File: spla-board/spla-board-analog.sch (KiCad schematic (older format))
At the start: 91 parts, among them J13 J_ANALOG, J14 J_AREF, J8 J_AREF_AMP, U51 ADC1173, U52 ADC1173, U53 ADC1173, U61 LMH6611, U62 LMH6611, U63 LMH6611, U74 LMH6611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

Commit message: schematic: Add Digikey and ManufacturerId fields to big components.
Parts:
- U51, U52, U53: Digikey (none) -> 296-35234-1-ND; Manufacturer Id (none) -> ADC1173CIMTCX/NOPB
- U61, U62, U63, U74, U75: Digikey (none) -> 296-41441-1-ND; Manufacturer Id (none) -> LMH6611MK/NOPB
- U76: Digikey (none) -> 296-40673-1-ND; Manufacturer Id (none) -> TLV73333PDBVR
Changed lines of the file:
@@
 F 2 "Package_SO:TSSOP-24_4.4x7.8mm_P0.65mm" H 14300 2550 50  0001 C CNN
 F 3 "http://www.ti.com/lit/ds/symlink/adc1173.pdf" H 14300 2550 50  0001 C CNN
+F 4 "296-35234-1-ND" H 14300 2550 50  0001 C CNN "Digikey"
+F 5 "ADC1173CIMTCX/NOPB" H 14300 2550 50  0001 C CNN "Manufacturer Id"
 	1    14300 2550
 	1    0    0    -1
@@
 F 2 "Package_SO:TSSOP-24_4.4x7.8mm_P0.65mm" H 14300 8650 50  0001 C CNN
 F 3 "http://www.ti.com/lit/ds/symlink/adc1173.pdf" H 14300 8650 50  0001 C CNN
+F 4 "296-35234-1-ND" H 14300 8650 50  0001 C CNN "Digikey"
+F 5 "ADC1173CIMTCX/NOPB" H 14300 8650 50  0001 C CNN "Manufacturer Id"
 	1    14300 8650
 	1    0    0    -1
@@
 F 2 "Package_SO:TSSOP-24_4.4x7.8mm_P0.65mm" H 14300 5600 50  0001 C CNN
 F 3 "http://www.ti.com/lit/ds/symlink/adc1173.pdf" H 14300 5600 50  0001 C CNN
+F 4 "296-35234-1-ND" H 14300 5600 50  0001 C CNN "Digikey"
+F 5 "ADC1173CIMTCX/NOPB" H 14300 5600 50  0001 C CNN "Manufacturer Id"
 	1    14300 5600
 	1    0    0    -1
@@
 F 2 "Package_TO_SOT_SMD:TSOT-23-6" H 9650 8000 50  0001 L CNN
 F 3 "http://www.ti.com/lit/ds/symlink/lmh6612.pdf" H 9700 8400 50  0001 C CNN
+F 4 "296-41441-1-ND" H 9550 8250 50  0001 C CNN "Digikey"
+F 5 "LMH6611MK/NOPB" H 9550 8250 50  0001 C CNN "Manufacturer Id"
 	1    9550 8250
 	1    0    0    -1
@@
 F 2 "Package_TO_SOT_SMD:TSOT-23-6" H 9650 1900 50  0001 L CNN
 F 3 "http://www.ti.com/lit/ds/symlink/lmh6612.pdf" H 9700 2300 50  0001 C CNN
+F 4 "296-41441-1-ND" H 9550 2150 50  0001 C CNN "Digikey"
+F 5 "LMH6611MK/NOPB" H 9550 2150 50  0001 C CNN "Manufacturer Id"
 	1    9550 2150
 	1    0    0    -1
@@
 F 2 "Package_TO_SOT_SMD:TSOT-23-6" H 9650 4950 50  0001 L CNN
 F 3 "http://www.ti.com/lit/ds/symlink/lmh6612.pdf" H 9700 5350 50  0001 C CNN
+F 4 "296-41441-1-ND" H 9550 5200 50  0001 C CNN "Digikey"
+F 5 "LMH6611MK/NOPB" H 9550 5200 50  0001 C CNN "Manufacturer Id"
 	1    9550 5200
 	1    0    0    -1
@@
 F 2 "Package_TO_SOT_SMD:TSOT-23-6" H 4400 7100 50  0001 L CNN
 F 3 "http://www.ti.com/lit/ds/symlink/lmh6612.pdf" H 4450 7500 50  0001 C CNN
+F 4 "296-41441-1-ND" H 4300 7350 50  0001 C CNN "Digikey"
+F 5 "LMH6611MK/NOPB" H 4300 7350 50  0001 C CNN "Manufacturer Id"
 	1    4300 7350
 	1    0    0    -1
@@
 F 2 "Package_TO_SOT_SMD:TSOT-23-6" H 4400 9650 50  0001 L CNN
 F 3 "http://www.ti.com/lit/ds/symlink/lmh6612.pdf" H 4450 10050 50  0001 C CNN
+F 4 "296-41441-1-ND" H 4300 9900 50  0001 C CNN "Digikey"
+F 5 "LMH6611MK/NOPB" H 4300 9900 50  0001 C CNN "Manufacturer Id"
 	1    4300 9900
 	1    0    0    -1
@@
 F 2 "Package_TO_SOT_SMD:SOT-23-5" H 2000 7100 50  0001 C CNN
 F 3 "http://www.ti.com/lit/ds/symlink/tlv733p.pdf" H 2100 6650 50  0001 C CNN
+F 4 "296-40673-1-ND" H 2000 6900 50  0001 C CNN "Digikey"
+F 5 "TLV73333PDBVR" H 2000 6900 50  0001 C CNN "Manufacturer Id"
 	1    2000 6900
 	1    0    0    -1

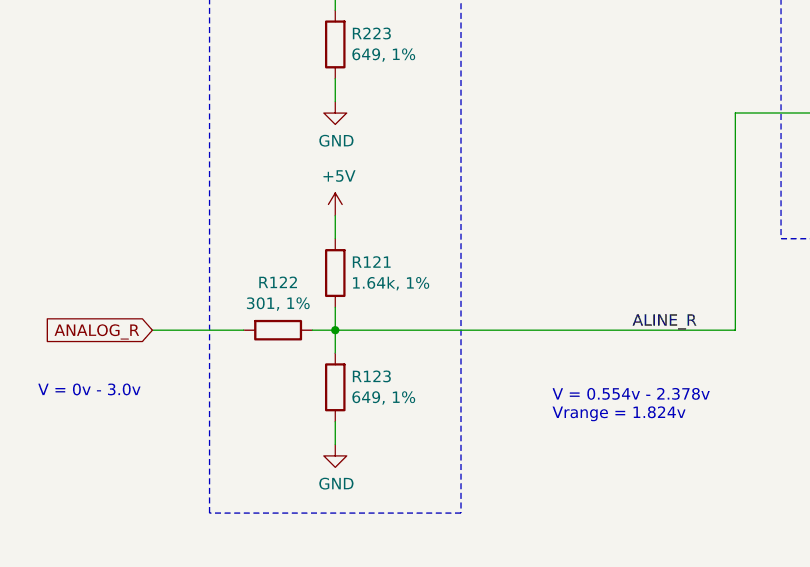
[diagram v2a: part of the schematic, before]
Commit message: schematic: Fix typo'd resistor value.
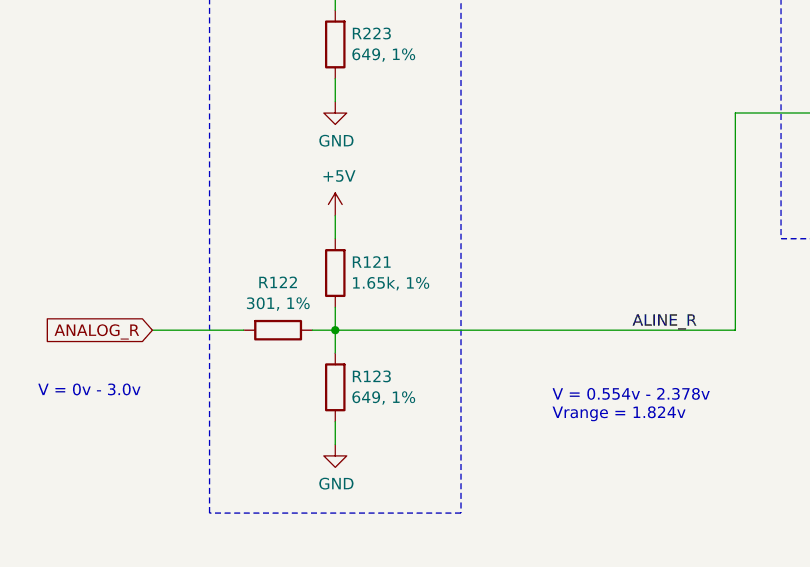
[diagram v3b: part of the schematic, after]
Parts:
- R121: value 1.64k, 1% -> 1.65k, 1%
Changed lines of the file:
@@
 P 2050 4250
 F 0 "R121" H 1980 4204 50  0000 R CNN
-F 1 "1.64k, 1%" H 1980 4295 50  0000 R CNN
+F 1 "1.65k, 1%" H 1980 4295 50  0000 R CNN
 F 2 "Resistor_SMD:R_0603_1608Metric" V 1980 4250 50  0001 C CNN
 F 3 "~" H 2050 4250 50  0001 C CNN

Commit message: schematic: Set 'N/A' for test points and holes 'parts'.
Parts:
- TP3, TP4: Digikey (none) -> N/A; Manufacturer Id (none) -> N/A
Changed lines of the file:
@@
 F 2 "TestPoint:TestPoint_Pad_D1.0mm" H 6400 8700 50  0001 C CNN
 F 3 "~" H 6400 8700 50  0001 C CNN
+F 4 "N/A" H 6200 8700 50  0001 C CNN "Digikey"
+F 5 "N/A" H 6200 8700 50  0001 C CNN "Manufacturer Id"
 	1    6200 8700
 	1    0    0    -1
@@
 F 2 "TestPoint:TestPoint_Pad_D1.0mm" H 6400 8900 50  0001 C CNN
 F 3 "~" H 6400 8900 50  0001 C CNN
+F 4 "N/A" H 6200 8900 50  0001 C CNN "Digikey"
+F 5 "N/A" H 6200 8900 50  0001 C CNN "Manufacturer Id"
 	1    6200 8900
 	-1   0    0    1

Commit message: schematic: Add part numbers for pinheaders (albeit that these are breakaways, and it's not one-per-part).
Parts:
- J13, J14, J8: Digikey (none) -> S2011EC-40-ND; Manufacturer Id (none) -> PRPC040DAAN-RC
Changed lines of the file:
@@
 F 2 "Connector_PinHeader_2.54mm:PinHeader_2x04_P2.54mm_Vertical" H 2100 8850 50  0001 C CNN
 F 3 "~" H 2100 8850 50  0001 C CNN
+F 4 "S2011EC-40-ND" H 2100 8850 50  0001 C CNN "Digikey"
+F 5 "PRPC040DAAN-RC" H 2100 8850 50  0001 C CNN "Manufacturer Id"
 	1    2100 8850
 	1    0    0    -1
@@
 F 2 "Connector_PinHeader_2.54mm:PinHeader_2x03_P2.54mm_Vertical" H 6250 3000 50  0001 C CNN
 F 3 "~" H 6250 3000 50  0001 C CNN
+F 4 "S2011EC-40-ND" H 6250 3000 50  0001 C CNN "Digikey"
+F 5 "PRPC040DAAN-RC" H 6250 3000 50  0001 C CNN "Manufacturer Id"
 	1    6250 3000
 	1    0    0    -1
@@
 F 2 "Connector_PinHeader_2.54mm:PinHeader_2x02_P2.54mm_Vertical" H 5800 8800 50  0001 C CNN
 F 3 "~" H 5800 8800 50  0001 C CNN
+F 4 "S2011EC-40-ND" H 5800 8800 50  0001 C CNN "Digikey"
+F 5 "PRPC040DAAN-RC" H 5800 8800 50  0001 C CNN "Manufacturer Id"
 	1    5800 8800
 	1    0    0    -1

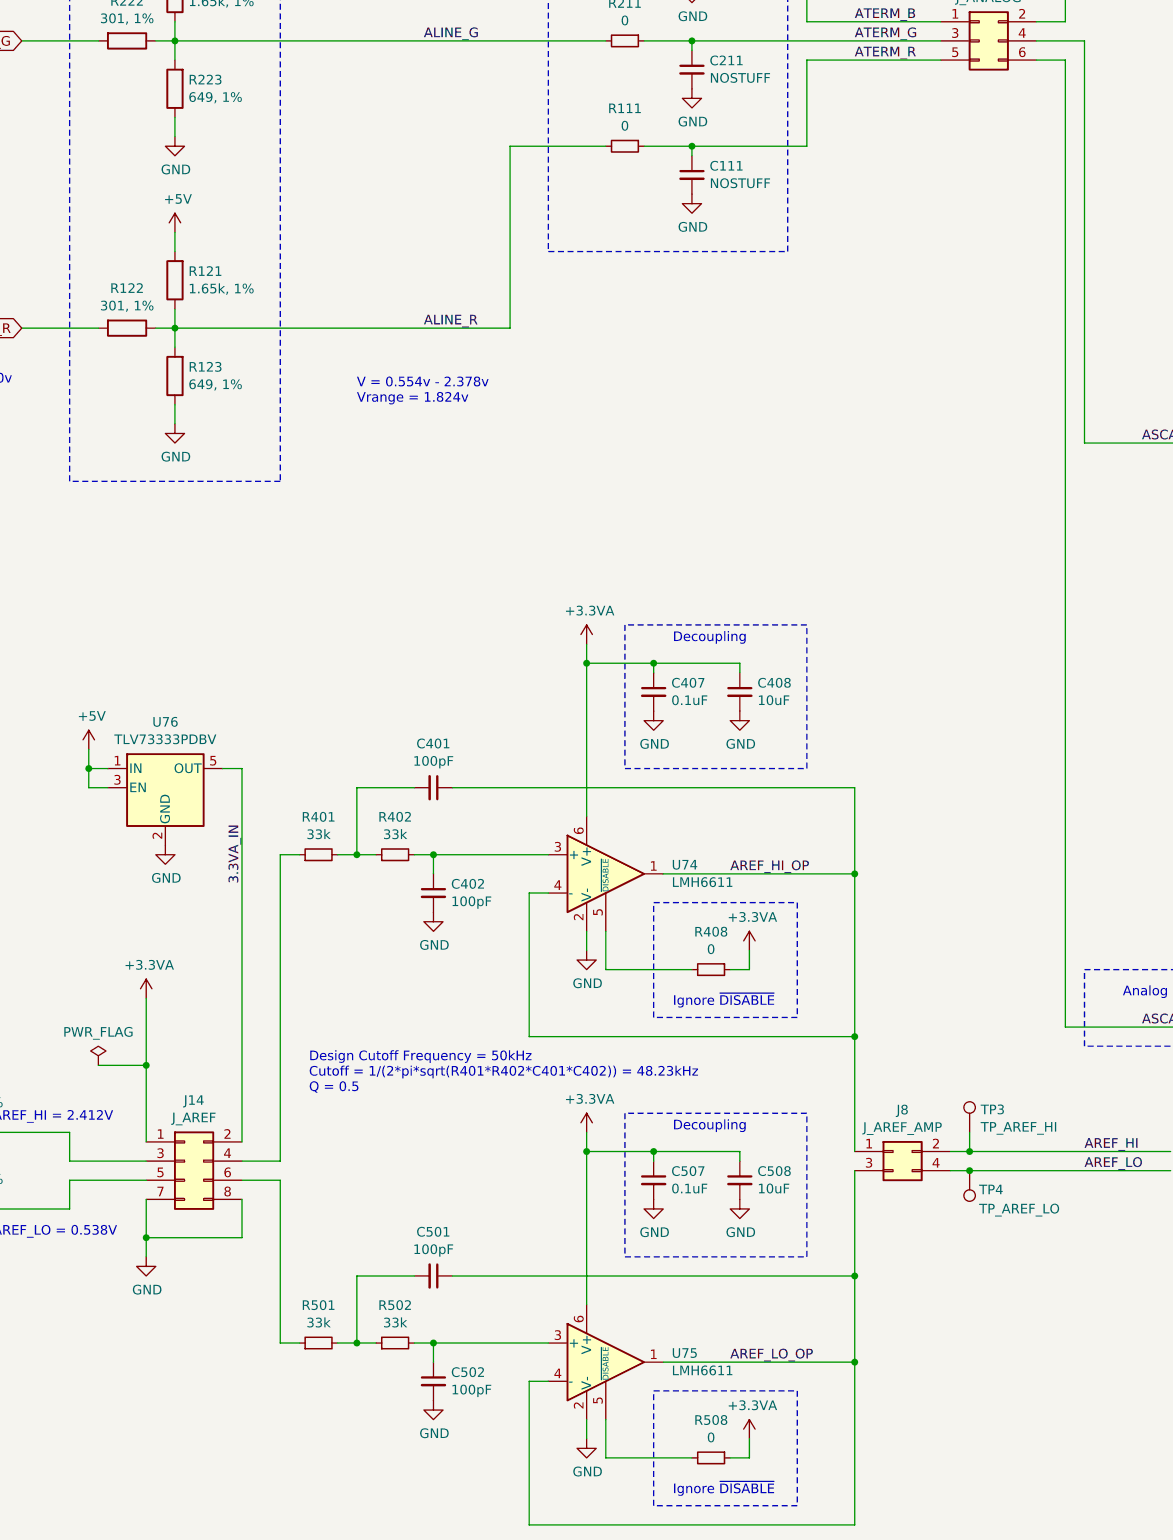
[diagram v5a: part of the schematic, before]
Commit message: schematic/pcb: Add BoM-only symbols.
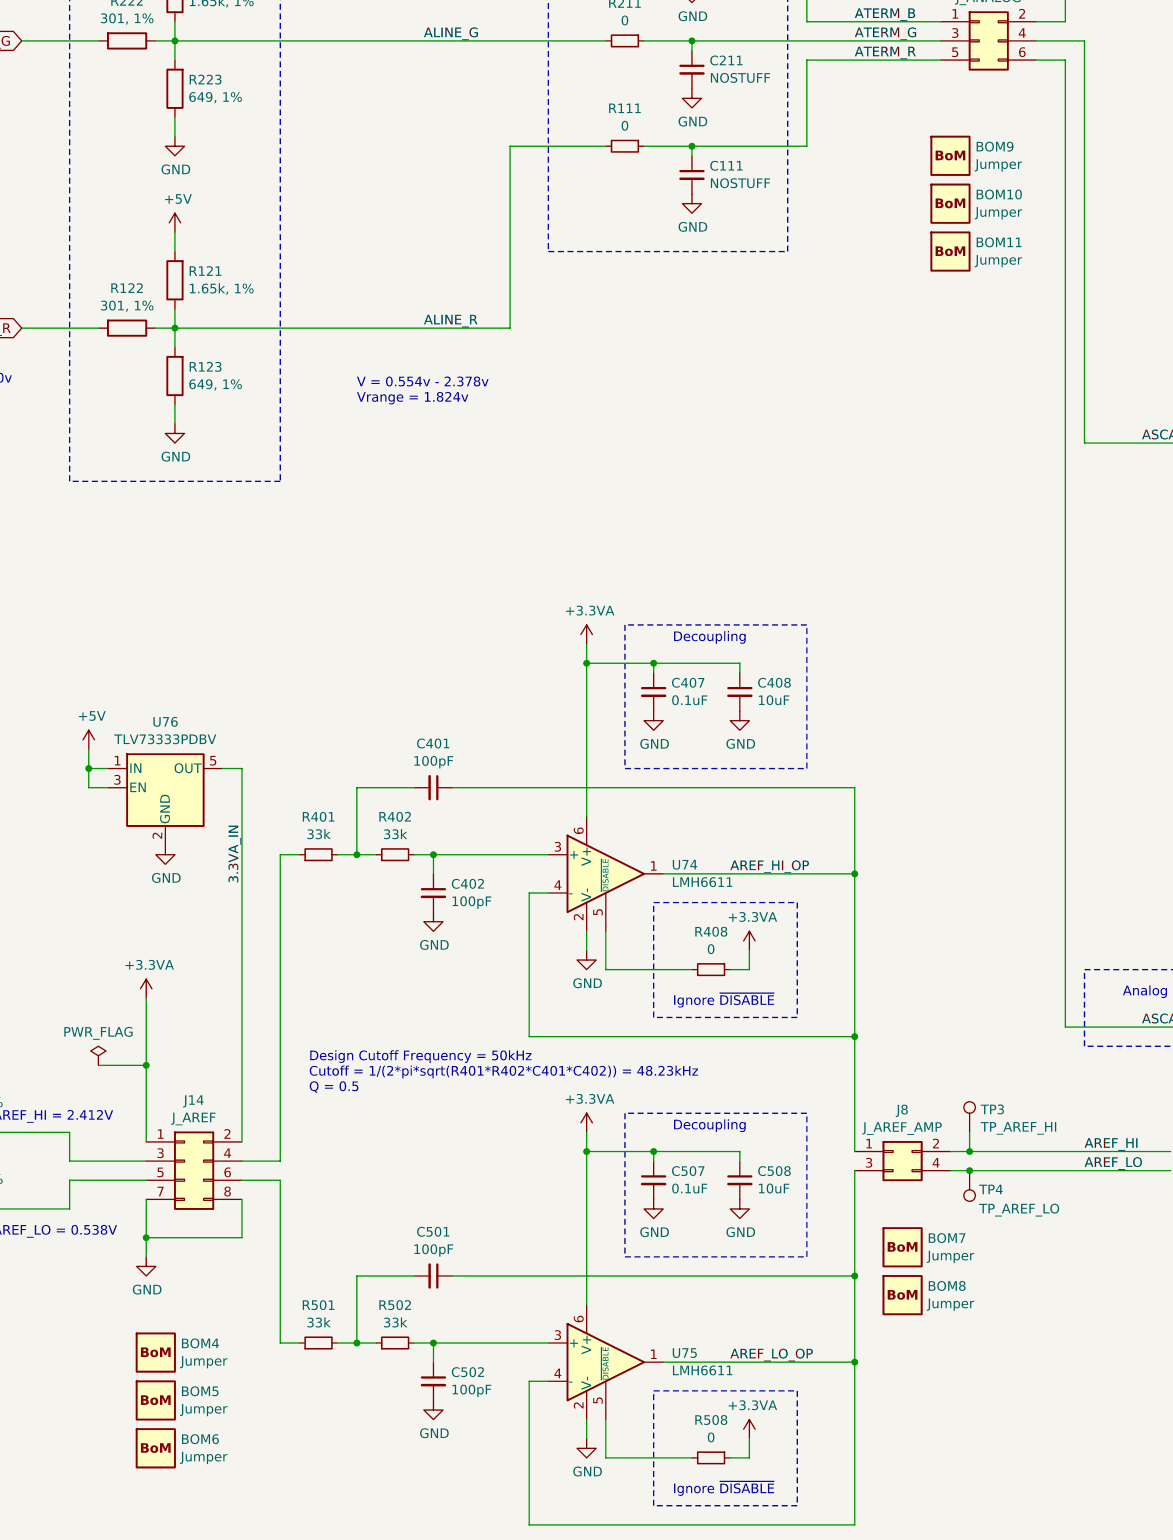
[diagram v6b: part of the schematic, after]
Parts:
- added BOM10, BOM11, BOM4, BOM5, BOM6, BOM7, BOM8, BOM9: Jumper, SPLA:BoM, symbol SPLA:BomExtra
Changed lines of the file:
@@
 	4550 8800 5000 8800
 Connection ~ 4550 8800
+$Comp
+L SPLA:BomExtra BOM?
+U 1 1 5EB18261
+P 1950 9850
+AR Path="/5E50E589/5EB18261" Ref="BOM?"  Part="1"
+AR Path="/5E520B87/5EB18261" Ref="BOM4"  Part="1"
+F 0 "BOM4" H 2080 9896 50  0000 L CNN
+F 1 "Jumper" H 2080 9805 50  0000 L CNN
+F 2 "SPLA:BoM" H 1950 9850 50  0001 C CNN
+F 3 "" H 1950 9850 50  0001 C CNN
+F 4 "S9337-ND" H 1950 9850 50  0001 C CNN "Digikey"
+F 5 "QPC02SXGN-RC" H 1950 9850 50  0001 C CNN "Manufacturer Id"
+	1    1950 9850
+	1    0    0    -1
+$EndComp
+$Comp
+L SPLA:BomExtra BOM?
+U 1 1 5EB36CC8
+P 1950 10100
+AR Path="/5E50E589/5EB36CC8" Ref="BOM?"  Part="1"
+AR Path="/5E520B87/5EB36CC8" Ref="BOM5"  Part="1"
+F 0 "BOM5" H 2080 10146 50  0000 L CNN
+F 1 "Jumper" H 2080 10055 50  0000 L CNN
+F 2 "SPLA:BoM" H 1950 10100 50  0001 C CNN
+F 3 "" H 1950 10100 50  0001 C CNN
+F 4 "S9337-ND" H 1950 10100 50  0001 C CNN "Digikey"
+F 5 "QPC02SXGN-RC" H 1950 10100 50  0001 C CNN "Manufacturer Id"
+	1    1950 10100
+	1    0    0    -1
+$EndComp
+$Comp
+L SPLA:BomExtra BOM?
+U 1 1 5EB558F5
+P 1950 10350
+AR Path="/5E50E589/5EB558F5" Ref="BOM?"  Part="1"
+AR Path="/5E520B87/5EB558F5" Ref="BOM6"  Part="1"
+F 0 "BOM6" H 2080 10396 50  0000 L CNN
+F 1 "Jumper" H 2080 10305 50  0000 L CNN
+F 2 "SPLA:BoM" H 1950 10350 50  0001 C CNN
+F 3 "" H 1950 10350 50  0001 C CNN
+F 4 "S9337-ND" H 1950 10350 50  0001 C CNN "Digikey"
+F 5 "QPC02SXGN-RC" H 1950 10350 50  0001 C CNN "Manufacturer Id"
+	1    1950 10350
+	1    0    0    -1
+$EndComp
+$Comp
+L SPLA:BomExtra BOM?
+U 1 1 5EB744FF
+P 5850 9300
+AR Path="/5E50E589/5EB744FF" Ref="BOM?"  Part="1"
+AR Path="/5E520B87/5EB744FF" Ref="BOM7"  Part="1"
+F 0 "BOM7" H 5980 9346 50  0000 L CNN
+F 1 "Jumper" H 5980 9255 50  0000 L CNN
+F 2 "SPLA:BoM" H 5850 9300 50  0001 C CNN
+F 3 "" H 5850 9300 50  0001 C CNN
+F 4 "S9337-ND" H 5850 9300 50  0001 C CNN "Digikey"
+F 5 "QPC02SXGN-RC" H 5850 9300 50  0001 C CNN "Manufacturer Id"
+	1    5850 9300
+	1    0    0    -1
+$EndComp
+$Comp
+L SPLA:BomExtra BOM?
+U 1 1 5EB7450B
+P 5850 9550
+AR Path="/5E50E589/5EB7450B" Ref="BOM?"  Part="1"
+AR Path="/5E520B87/5EB7450B" Ref="BOM8"  Part="1"
+F 0 "BOM8" H 5980 9596 50  0000 L CNN
+F 1 "Jumper" H 5980 9505 50  0000 L CNN
+F 2 "SPLA:BoM" H 5850 9550 50  0001 C CNN
+F 3 "" H 5850 9550 50  0001 C CNN
+F 4 "S9337-ND" H 5850 9550 50  0001 C CNN "Digikey"
+F 5 "QPC02SXGN-RC" H 5850 9550 50  0001 C CNN "Manufacturer Id"
+	1    5850 9550
+	1    0    0    -1
+$EndComp
+$Comp
+L SPLA:BomExtra BOM?
+U 1 1 5EB936B5
+P 6100 3600
+AR Path="/5E50E589/5EB936B5" Ref="BOM?"  Part="1"
+AR Path="/5E520B87/5EB936B5" Ref="BOM9"  Part="1"
+F 0 "BOM9" H 6230 3646 50  0000 L CNN
+F 1 "Jumper" H 6230 3555 50  0000 L CNN
+F 2 "SPLA:BoM" H 6100 3600 50  0001 C CNN
+F 3 "" H 6100 3600 50  0001 C CNN
+F 4 "S9337-ND" H 6100 3600 50  0001 C CNN "Digikey"
+F 5 "QPC02SXGN-RC" H 6100 3600 50  0001 C CNN "Manufacturer Id"
+	1    6100 3600
+	1    0    0    -1
+$EndComp
+$Comp
+L SPLA:BomExtra BOM?
+U 1 1 5EBB26B8
+P 6100 3850
+AR Path="/5E50E589/5EBB26B8" Ref="BOM?"  Part="1"
+AR Path="/5E520B87/5EBB26B8" Ref="BOM10"  Part="1"
+F 0 "BOM10" H 6230 3896 50  0000 L CNN
+F 1 "Jumper" H 6230 3805 50  0000 L CNN
+F 2 "SPLA:BoM" H 6100 3850 50  0001 C CNN
+F 3 "" H 6100 3850 50  0001 C CNN
+F 4 "S9337-ND" H 6100 3850 50  0001 C CNN "Digikey"
+F 5 "QPC02SXGN-RC" H 6100 3850 50  0001 C CNN "Manufacturer Id"
+	1    6100 3850
+	1    0    0    -1
+$EndComp
+$Comp
+L SPLA:BomExtra BOM?
+U 1 1 5EBD1242
+P 6100 4100
+AR Path="/5E50E589/5EBD1242" Ref="BOM?"  Part="1"
+AR Path="/5E520B87/5EBD1242" Ref="BOM11"  Part="1"
+F 0 "BOM11" H 6230 4146 50  0000 L CNN
+F 1 "Jumper" H 6230 4055 50  0000 L CNN
+F 2 "SPLA:BoM" H 6100 4100 50  0001 C CNN
+F 3 "" H 6100 4100 50  0001 C CNN
+F 4 "S9337-ND" H 6100 4100 50  0001 C CNN "Digikey"
+F 5 "QPC02SXGN-RC" H 6100 4100 50  0001 C CNN "Manufacturer Id"
+	1    6100 4100
+	1    0    0    -1
+$EndComp
 $EndSCHEMATC
